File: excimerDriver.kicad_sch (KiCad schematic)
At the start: 39 parts, among them IC3 INA210, IC6 STM32G071KBT6, J1 B08B-XASK-1-A_LF__SN_, J3 BM02B-SRSS-TB_LF__SN_, J4 BM02B-SRSS-TB_LF__SN_, J6 640445-2, Q3 BSS138, U3 LM2902, U4 Prog

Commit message: alpha prototype
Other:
- note added: "Gain = 0.02 * 200 = 4"
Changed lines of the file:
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@@
 	(generator_version "9.99")
 	(paper "A4")
+	(text "Gain = 0.02 * 200 = 4"
+		(exclude_from_sim no)
+		(at 150.368 56.642 0)
+		(effects
+			(font
+				(size 1.27 1.27)
+			)
+		)
+	)
 	(junction
 		(at 82.55 25.4)
@@
 			"AAAAAAAAAAAAAAAAAAAAAAAAAAAAAAAAAAAAAAAAAAAAAAAAAAAAAAAAAAAAAAAAAAAAAAAAAAAA"
 			"AAAAAAAAAAAAAAAAAAAAAAAAAAAAAAAAAAAAAAAAAAAAAAAAAAAAAAAAAAAAAAAAAAAAAAAAAAAA"
-			"AAAAAAAAAAAAAAAAAA=="
-		)
-	)
+			"AAAAAAAAAAAAAAAAAAAAAAAAAAAAAAAAAAAAAAAAAAAAAAAAAAAAAAAAAAAAAAAAAAAAAAAAAAAA"
+			"AAAAAAAAAAAAAAAAAAAAAAAAAAAAAAAAAAAAAAAAAAAAAAAAAAAAAAAAAAAAAAAAAAAAAAAAAAAA"
+			"AAAAAAAAAAAAAAAAAAAAAAAAAAAAAAAAAAAAAAAAAAAAAAAAAAAAAAAAAAAAAAAAAAAAAAAAAAAA"
+			"AAAAAAAAAAAAAAAAAAAAAAAAAAAAAAAAAAAAAAAAAAAAAAAAAAAAAAAAAAAAAAAAAAAAAAAAAAAA"
+			"AAAAAAAAAAAAAAAAAAAAAAAAAAAAAAAAAAAAAAAAAAAAAAAAAAAAAAAAAAAAAAAAAAAAAAAAAAAA"
+			"AAAAAAAAAAAAAAAAAAAAAAAAAAAAAAAAAAAAAAAAAAAAAAAAAAAAAAAAAAAAAAAAAAAAAAAAAAAA"
+			"AAAAAAAAAAAAAAAAAAAAAAAAAAAAAAAAAAAAAAAAAAAAAAAAAAAAAAAAAAAAAAAAAAAAAAAAAAAA"
+			"AAAAAAAAAAAAAAAAAAAAAAAAAAAAAAAAAAAAAAAAAAAAAAAAAAAAAAAAAAAAAAAAAAAAAAAAAAAA"
+			"AAAAAAAAAAAAAAAAAAAAAAAAAAAAAAAAAAAAAAAAAAAAAAAAAAAAAAAAAAAAAAAAAAAAAAAAAAAA"
+			"AAAAAAAAAAAAAAAAAAAAAAAAAAAAAAAAAAAAAAAAAAAAAAAAAAAAAAAAAAAAAAAAAAAAAAAAAAAA"
+			"AAAAAAAAAAAAAAAAAAAAAAAAAAAAAAAAAAAAAAAAAAAAAAAAAAAAAAAAAAAAAAAAAAAAAAAAAAAA"
+			"AAAAAAAAAAAAAAAAAAAAAAAAAAAAAAAAAAAAAAAAAAAAAAAAAAAAAAAAAAAAAAAAAAAAAAAAAAAA"
+			"AAAAAAAAAAAAAAAAAAAAAAAAAAAAAAAAAAAAAAAAAAAAAAAAAAAAAAAAAAAAAAAAAAAAAAAAAAAA"
+			"AAAAAAAAAAAAAAAAAAAAAAAAAAAAAAAAAAAAAAAAAAAAAAAAAAAAAAAAAAAAAAAAAAAAAAAAAAAA"
+			"AAAAAAAAAAAAAAAAAAAAAAAAAAAAAAAAAAAAAAAAAAAAAAAAAAAAAAAAAAAAAAAAAAAAAAAAAAAA"
+			"AAAAAAAAAAAAAAAAAAAAAAAAAAAAAAAAAAAAAAAAAAAAAAAAAAAAAAAAAAAAAAAAAAAAAAAAAAAA"
+			"AAAAAAAAAAAAAAAAAAAAAAAAAAAAAAAAAAAAAAAAAAAAAAAAAAAAAAAAAAAAAAAAAAAAAAAAAAAA"
+			"AAAAAAAAAAAAAAAAAAAAAAAAAAAAAAAAAAAAAAAAAAAAAAAAAAAAAAAAAAAAAAAAAAAAAAAAAAAA"
+			"AAAAAAAAAAAAAAAAAP8AAAAAAACAPwAAAADg1KDsTAIAAAEAAAAAAAAAAAAAAAAAAAAAAAAAAAAA"
+			"AAAAAAAAAAAABwAAAAAAAAAIAAAAAAAAAAAAAAAAAAAAwPwx6UwCAAACAAAAAAAAAAAAAAAAAAAA"
+			"AAAAAAAAAAAAAAAAAAAAAAAAAAAAAAAAYfzidDteee8AAAAAAAAAAAAAAAAAAAAAAAAAAAAAAAAH"
+			"AAAAAAAAAAAAAAAAAAAAAAAAAAAAAAACAAAAAAAAAFAHCu1MAgAAAAAAAAAAAAAAAAAAAAAAANAB"
+			"MulMAgAAAAAAAAAAAAACAAAAAAAAAAAAAAAAAAAAAAAAAAAAAAAAAAAAAAAAAAAAAAAAAAAAAAAA"
+			"AAAAAAAAAAAAAAAAAAAAAAAAAAAAAAAAAAAAAAD/////AAAAAAAAAAAAAAAAK6BYlwAVAIAARZnL"
+			"TAIAAAAAAAAAAAAAAAAAAAAAAADg1jHpTAIAAAAAAAAAAAAAPgAAAAEBAQAAAAAAAAAAAEDXMelM"
+			"AgAAAAAAAAAAAAAAAIA/AAAAACBeMelMAgAAAAAAAAAAAAAAAAAAAAAAAAAAAAAAAAAAAAAAAAAA"
+			"AAAHAAAAAAAAAAgAAAAAAAAAAACAPwAAAAAAUTHpTAIAAAAAAAAAAAAAAAAAAAAAAAAAAAAAAAAA"
+			"AAAAAAAAAAAABwAAAAAAAAAIAAAAAAAAALDTMelMAgAAAAAAAAAAAABg2DHpTAIAAAAAAAAAAAAA"
+			"4IBp2EwCAAAAAIA/AAAAAACKpupMAgAAAAAAAAAAAAAAAAAAAAAAAAAAAAAAAAAAAAAAAAAAAAAH"
+			"AAAAAAAAAAgAAAAAAAAAAgAAAAAAAAAAAAAAAAAAAAAAAAAAAAAAAAAAAAAAAAAAAAAAAAAAAAAA"
+			"AAAAAAAAAAAAAAAAAAAAAAAAAAAAAAAAAAAAAAAA/////wAAAAAAAIA/AAAAADCb08xMAgAAAAAA"
+			"AAAAAAAAAAAAAAAAAAAAAAAAAAAAAAAAAAAAAAAHAAAAAAAAAAgAAAAAAAAAAAAAAAAAAADQ1DHp"
+			"TAIAAAAAAAAAAAAAAAAAAAAAAAAAAAAAAAAAAAAAAAAAAAAAAAAAAAAAAABh/OJ0O1557wAAAAAA"
+			"AAAAAAAAAAAAAAAAAAAAAAAAAAcAAAAAAAAAAAAAAAAAAAAAAAAAAAAAAAIAAAAAAAAAYOgJ7UwC"
+			"AAAAAAAAAAAAAAAAAAAAAAAA8NUx6UwCAAAAAAAAAAAAAAIAAAAAAAAAAAAAAAAAAAAAAAAAAAAA"
+			"AAAAAAAAAAAAAAAAAAAAAAAAAAAAAAAAAAAAAAAAAAAAAAAAAAAAAAAAAAAAAAAAAP////8AAAAA"
+			"AAAAAAAAAAB/oDSXAA=="
+		)
+	)

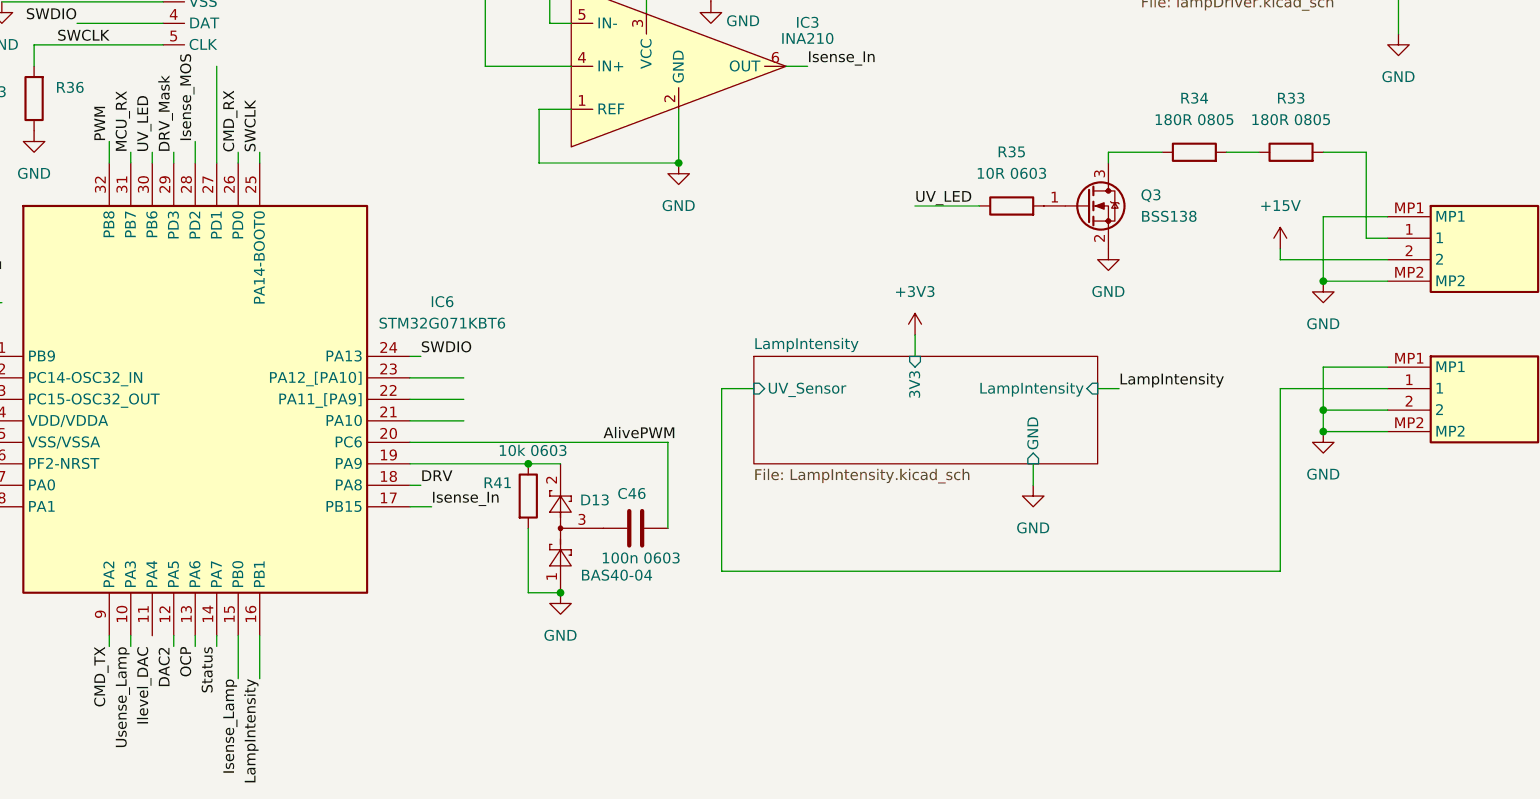
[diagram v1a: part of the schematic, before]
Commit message: error correction first prototype
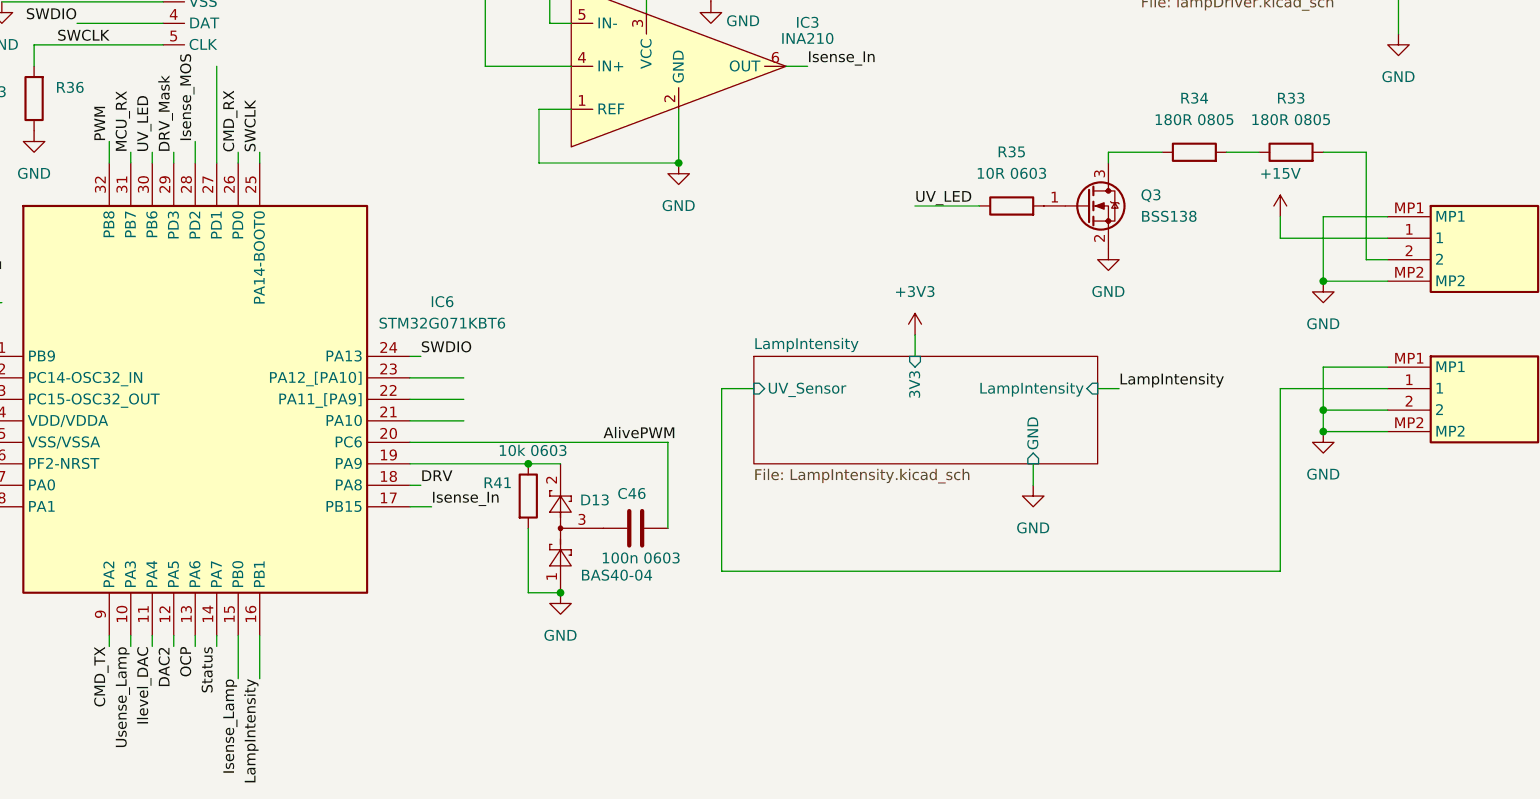
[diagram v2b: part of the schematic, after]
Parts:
- IC3: footprint Hansmann:SOT95P280X90-6N -> Package_TO_SOT_SMD:SOT-363_SC-70-6
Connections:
- net +15V: now also J3.1; no longer J3.2
- net Ilevel_DAC: now also IC6.11 (PA4)
- net at R33.2: now also J3.2; no longer J3.1

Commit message: etd29 transformer single layer
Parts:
- removed U3: LM2902, Package_SO:TSSOP-14_4.4x5mm_P0.65mm, symbol Amplifier_Operational:LM2902
- added C2: 100n 0603, Capacitor_SMD:C_0603_1608Metric, symbol Device:C
- added R72: 1k 0603, Resistor_SMD:R_0603_1608Metric, symbol Device:R
- C110: footprint Capacitor_THT:CP_Radial_D13.0mm_P5.00mm -> Capacitor_THT:CP_Radial_D8.0mm_P5.00mm
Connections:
- net +15V: now also J3.2; no longer J3.1
- net GND: now also C2.2
- net Isense_In: now also C2.1, R72.1; no longer IC3.6 (OUT)
- net at R33.2: now also J3.1; no longer J3.2
- new net: IC3.6 (OUT), R72.2

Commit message: V2 PCB
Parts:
- removed D12: LED gr 0603, LED_SMD:LED_0603_1608Metric, symbol Device:LED
- removed R38: 1k5 0603, Resistor_SMD:R_0603_1608Metric, symbol Device:R
- J1: footprint B08BXASK1ALFSN -> Hansmann:B08BXASK1ALFSN
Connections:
- net +15V: no longer J3.2
- net DRV_Mask: now also IC6.32 (PB8); no longer IC6.29 (PD3)
- net PWM: now also IC6.29 (PD3); no longer IC6.32 (PB8)
- net 24V_FUSE: now reaches C110.1, D21.1 (K), F2.2, L3.1
- net 24V_FUSE: now also J3.2
- net DAC2: no longer names the net of IC6.12 (PA5)
- net Ilevel_DAC: no longer names the net of IC6.11 (PA4)
- net MCU_RX: no longer names the net of IC6.31 (PB7)

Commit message: Beta Prototype production data, KiCad Stable version
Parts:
- added R45: 0R02 1% 1206, Resistor_SMD:R_1206_3216Metric, symbol Device:R
- added TP1, TP2, TP3, TP4, TP5, TP6, TP8, TP9: TestPoint, TestPoint:TestPoint_Pad_D1.0mm, symbol Connector:TestPoint
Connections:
- net +15V: now also TP8.1
- net +3V3: now also TP9.1
- net 24V_FUSE: now also TP1.1
- net 24V_Sense: now also TP4.1
- net GND: now also R45.2
- net Isense_In: now also TP5.1
- net VDC_filter: now also R45.1, TP2.1
- net VDC_power: now also TP3.1
- net at Q3.3 (D), R34.1: now also TP6.1
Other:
- moved on the sheet: R35
